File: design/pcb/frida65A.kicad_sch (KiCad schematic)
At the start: 101 parts, among them J1 DisplayPort Molex 472720024, J10 VIN CFG, J11 TP AMP, J12 MiniFitJr Molex 469990014, J13 POWER, J14 RJ45 Molex 446200002, J15 SPI TP, J2 TP CLOCKS, J3 SMA Molex 733910070, J4 SMA Molex 733910070, J5 DIFF/SE CFG, J6 TERM CFG, J7 ATTEN CFG, J8 SMA Molex 733910070, J9 TERM CFG, Q1 Q_PMOS_GSD, U1 DiffAmp TI THS4541, U2 TI LevelShifter SN74AXC8T245R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, U3 ASIC FRIDA 65A

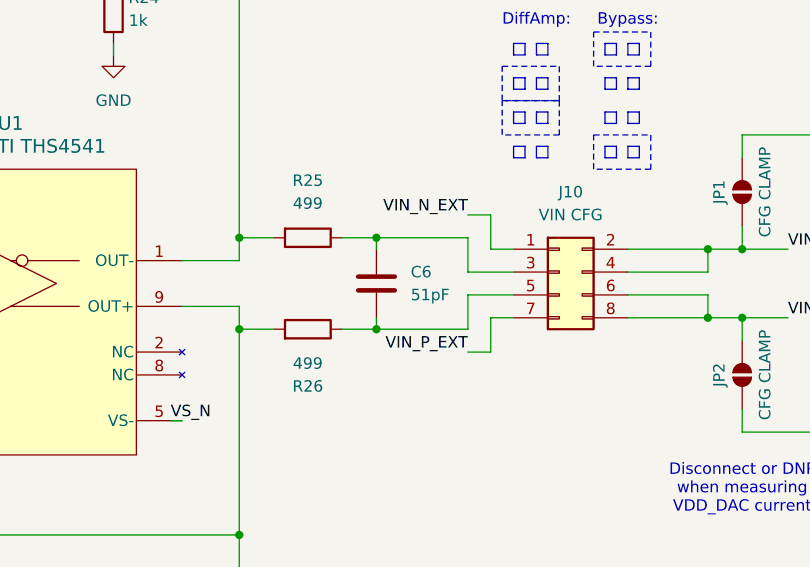
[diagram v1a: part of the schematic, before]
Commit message: fix(pcb): increase C6 decoupling capacitance
- Change C6 from 51 pF to 100 nF.\n- Preserve its rail connections after repositioning the symbol.
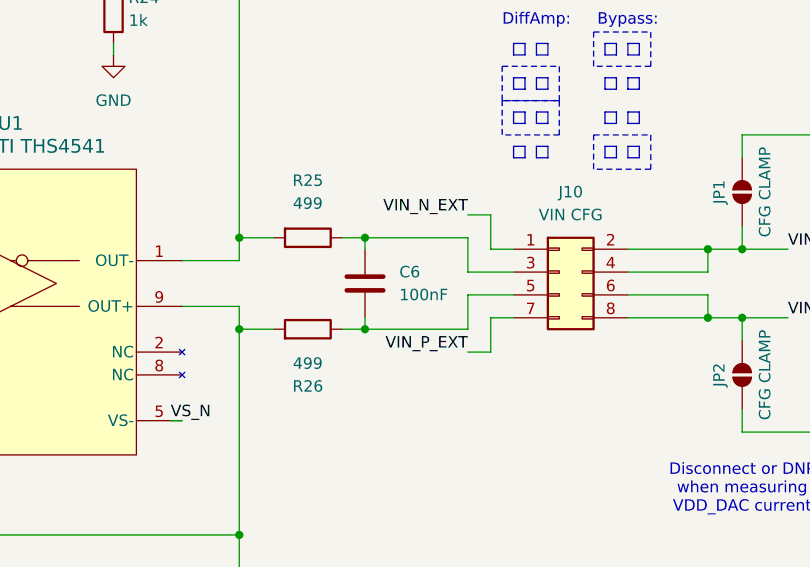
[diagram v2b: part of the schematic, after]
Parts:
- C6: value 51pF -> 100nF
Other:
- moved on the sheet: C6
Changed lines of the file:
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@@
 	)
 	(junction
+		(at 340.36 93.98)
+		(diameter 0)
+		(color 0 0 0 0)
+	)
+	(junction
 		(at 111.76 87.63)
 		(diameter 0)
@@
 	)
 	(junction
-		(at 341.63 83.82)
-		(diameter 0)
-		(color 0 0 0 0)
-	)
-	(junction
 		(at 119.38 95.25)
 		(diameter 0)
@@
 	)
 	(junction
-		(at 341.63 93.98)
-		(diameter 0)
-		(color 0 0 0 0)
-	)
-	(junction
 		(at 66.04 217.17)
 		(diameter 0)
@@
 	)
 	(junction
+		(at 340.36 83.82)
+		(diameter 0)
+		(color 0 0 0 0)
+	)
+	(junction
 		(at 116.84 267.97)
 		(diameter 0)
@@
 	(wire
 		(pts
-			(xy 337.82 93.98) (xy 341.63 93.98)
+			(xy 337.82 93.98) (xy 340.36 93.98)
 		)
 		(stroke
@@
 	(wire
 		(pts
-			(xy 341.63 83.82) (xy 341.63 85.09)
+			(xy 340.36 83.82) (xy 340.36 85.09)
 		)
 		(stroke
@@
 	(wire
 		(pts
-			(xy 337.82 83.82) (xy 341.63 83.82)
+			(xy 337.82 83.82) (xy 340.36 83.82)
 		)
 		(stroke
@@
 	(wire
 		(pts
-			(xy 341.63 83.82) (xy 351.79 83.82)
-		)
-		(stroke
-			(width 0)
-			(type default)
-		)
-	)
-	(wire
-		(pts
 			(xy 356.87 194.31) (xy 356.87 196.85)
 		)
@@
 	(wire
 		(pts
+			(xy 340.36 93.98) (xy 351.79 93.98)
+		)
+		(stroke
+			(width 0)
+			(type default)
+		)
+	)
+	(wire
+		(pts
 			(xy 205.74 60.96) (xy 212.09 60.96)
 		)
@@
 		)
 	)
-	(wire
-		(pts
-			(xy 341.63 93.98) (xy 351.79 93.98)
-		)
-		(stroke
-			(width 0)
-			(type default)
-		)
-	)
 	(polyline
 		(pts
@@
 	(wire
 		(pts
-			(xy 341.63 92.71) (xy 341.63 93.98)
+			(xy 340.36 92.71) (xy 340.36 93.98)
 		)
 		(stroke
@@
 	(wire
 		(pts
+			(xy 340.36 83.82) (xy 351.79 83.82)
+		)
+		(stroke
+			(width 0)
+			(type default)
+		)
+	)
+	(wire
+		(pts
 			(xy 185.42 181.61) (xy 179.07 181.61)
 		)
@@
 	(symbol
 		(lib_id "Device:C")
-		(at 341.63 88.9 0)
+		(at 340.36 88.9 0)
 		(unit 1)
 		(body_style 1)
@@
 		(fields_autoplaced yes)
 		(property "Reference" "C6"
-			(at 345.44 87.6299 0)
+			(at 344.17 87.6299 0)
 			(show_name no)
 			(do_not_autoplace no)
@@
 			)
 		)
-		(property "Value" "51pF"
-			(at 345.44 90.1699 0)
+		(property "Value" "100nF"
+			(at 344.17 90.1699 0)
 			(show_name no)
 			(do_not_autoplace no)
@@
 		)
 		(property "Footprint" "Capacitor_SMD:C_0402_1005Metric"
-			(at 342.5952 92.71 0)
+			(at 341.3252 92.71 0)
 			(hide yes)
 			(show_name no)
@@
 		)
 		(property "Datasheet" ""
-			(at 341.63 88.9 0)
+			(at 340.36 88.9 0)
 			(hide yes)
 			(show_name no)
@@
 		)
 		(property "Description" "Unpolarized capacitor"
-			(at 341.63 88.9 0)
+			(at 340.36 88.9 0)
 			(hide yes)
 			(show_name no)
@@
 		)
 		(property "Sim.Device" ""
-			(at 341.63 88.9 0)
+			(at 340.36 88.9 0)
 			(hide yes)
 			(show_name no)
@@
 		)
 		(property "Sim.Pins" ""
-			(at 341.63 88.9 0)
+			(at 340.36 88.9 0)
 			(hide yes)
 			(show_name no)
@@
 		)
 		(property "Sim.Type" ""
-			(at 341.63 88.9 0)
+			(at 340.36 88.9 0)
 			(hide yes)
 			(show_name no)
